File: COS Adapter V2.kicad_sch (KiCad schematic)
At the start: 18 parts, among them J1 COS Input, J2 COS Output, J3 12V Input, J8 Arcom Audio, J9 Radio Audio, K1 DIP Mini Relay, Q1 2N3906, U1 LM741

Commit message: added big pads
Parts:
- C1: footprint Capacitor_THT:C_Axial_L5.1mm_D3.1mm_P7.50mm_Horizontal -> Capacitor_THT:C_Axial_L5.1mm_D3.1mm_P7.50mm_Horizontal_BIG_FEET
- R3, R4: footprint Resistor_THT:R_Axial_DIN0204_L3.6mm_D1.6mm_P7.62mm_Horizontal -> Resistor_THT:R_Axial_DIN0204_L3.6mm_D1.6mm_P7.62mm_Horizontal_BIG_FEET
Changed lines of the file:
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@@
 			)
 		)
-		(property "Footprint" "Capacitor_THT:C_Axial_L5.1mm_D3.1mm_P7.50mm_Horizontal"
+		(property "Footprint" "Capacitor_THT:C_Axial_L5.1mm_D3.1mm_P7.50mm_Horizontal_BIG_FEET"
 			(at 64.77 114.3 0)
 			(effects
@@
 			)
 		)
-		(property "Footprint" "Resistor_THT:R_Axial_DIN0204_L3.6mm_D1.6mm_P7.62mm_Horizontal"
+		(property "Footprint" "Resistor_THT:R_Axial_DIN0204_L3.6mm_D1.6mm_P7.62mm_Horizontal_BIG_FEET"
 			(at 69.85 126.492 90)
 			(effects
@@
 			)
 		)
-		(property "Footprint" "Resistor_THT:R_Axial_DIN0204_L3.6mm_D1.6mm_P7.62mm_Horizontal"
+		(property "Footprint" "Resistor_THT:R_Axial_DIN0204_L3.6mm_D1.6mm_P7.62mm_Horizontal_BIG_FEET"
 			(at 55.88 110.998 90)
 			(effects

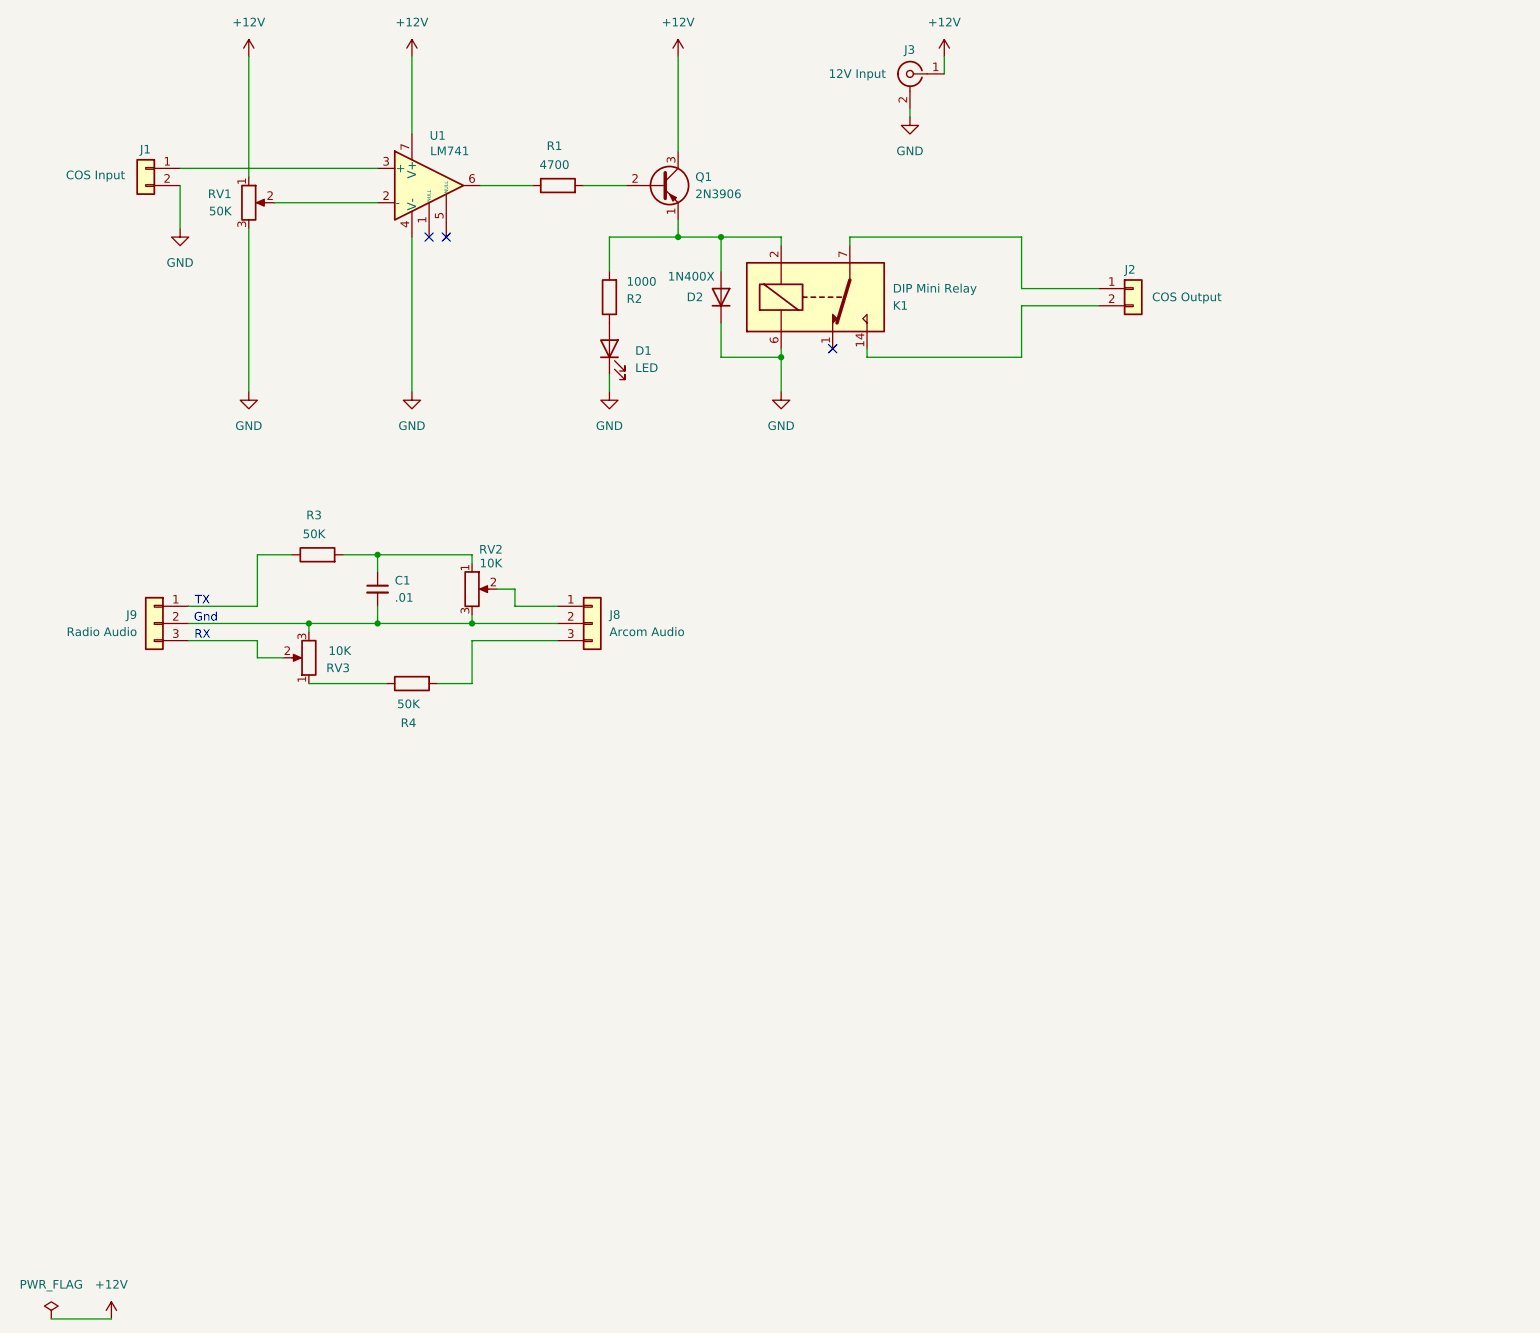
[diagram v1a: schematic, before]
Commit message: add Arcom mounting holes
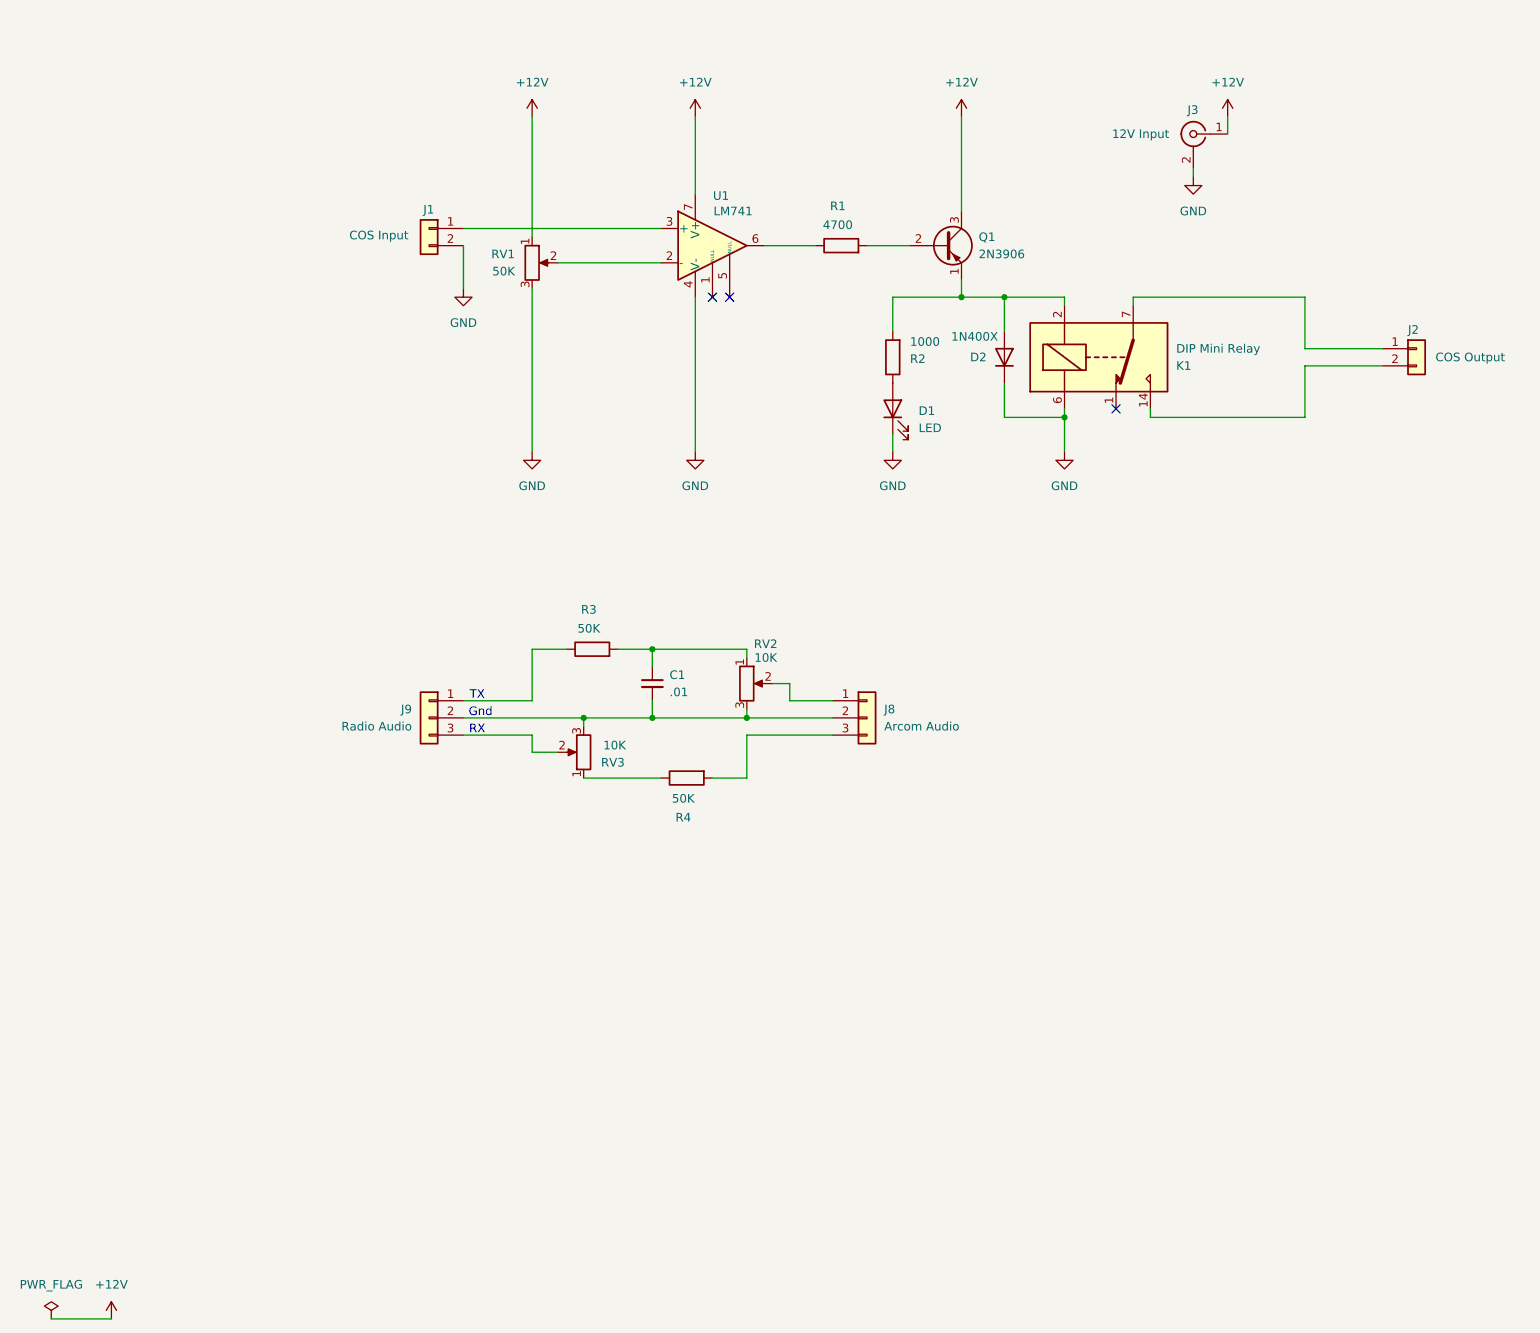
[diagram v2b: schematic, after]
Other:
- moved on the sheet: C1, D1, D2, J1, J2, J3, J8, J9, K1, Q1, R1, R2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

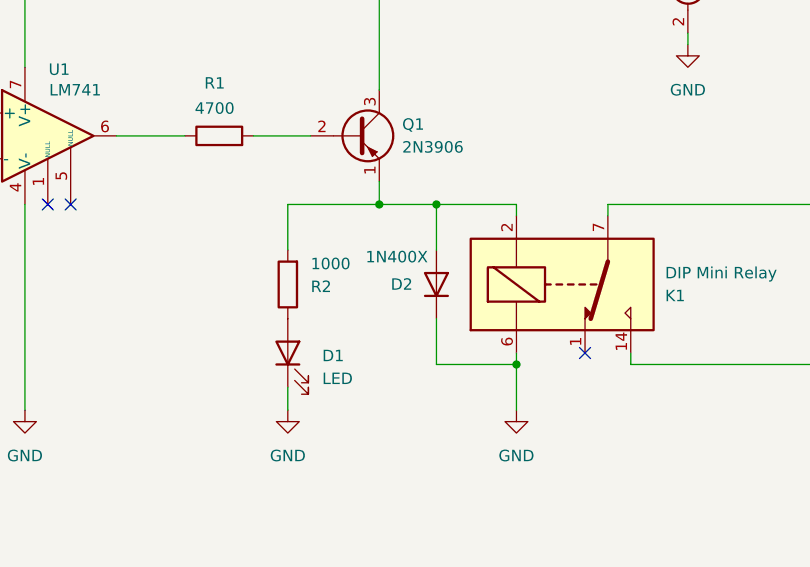
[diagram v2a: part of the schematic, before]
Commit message: v2.2: fix diode polarity
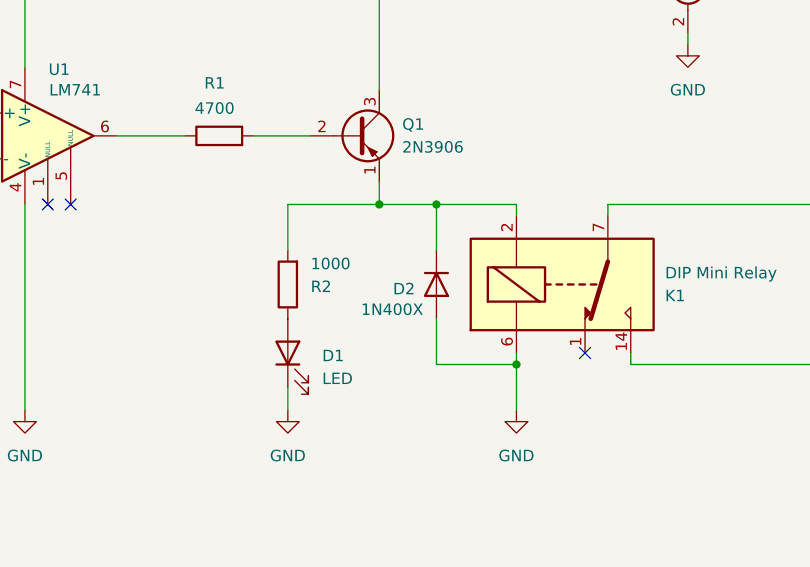
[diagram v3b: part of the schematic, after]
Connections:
- net GND: now also D2.2 (A); no longer D2.1 (K)
- net at K1.2, Q1.1 (E), R2.2: now also D2.1 (K); no longer D2.2 (A)
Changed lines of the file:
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@@
 		(title "COS Adapter V2")
 		(date "2026-01-14")
-		(rev "v2")
+		(rev "v2.2")
 		(company "David Kensiski W6DLK")
+		(comment 1 "v2.2: fixed diode polarity")
 		(comment 2 "Alternate holes for mounting inside Arcom")
 		(comment 3 "Fits 3.9x2.4 project box amazon.com/dp/B07D23C962/")
@@
 		(lib_id "Device:D")
 		(at 157.48 80.01 270)
-		(mirror x)
 		(unit 1)
 		(exclude_from_sim no)
@@
 		(dnp no)
 		(property "Reference" "D2"
-			(at 152.4 80.01 90)
+			(at 152.654 80.518 90)
 			(effects
 				(font
@@
 		)
 		(property "Value" "1N400X"
-			(at 149.606 76.962 90)
-			(effects
-				(font
+			(at 149.098 82.804 90)
+			(effects
+				(font
